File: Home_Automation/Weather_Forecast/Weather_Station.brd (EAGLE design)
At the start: 30 x 20 mm, 14 parts, among them U1 SHT4X, U2 DPS310

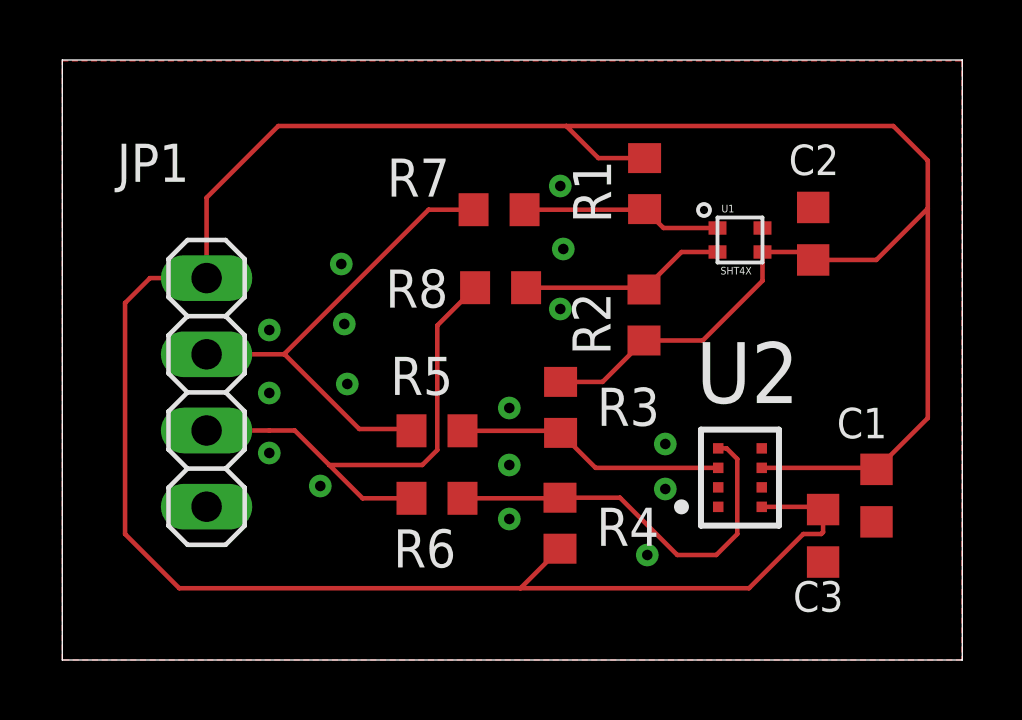
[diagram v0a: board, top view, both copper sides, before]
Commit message: New version: Re-design for better working and added a LED for indicating power
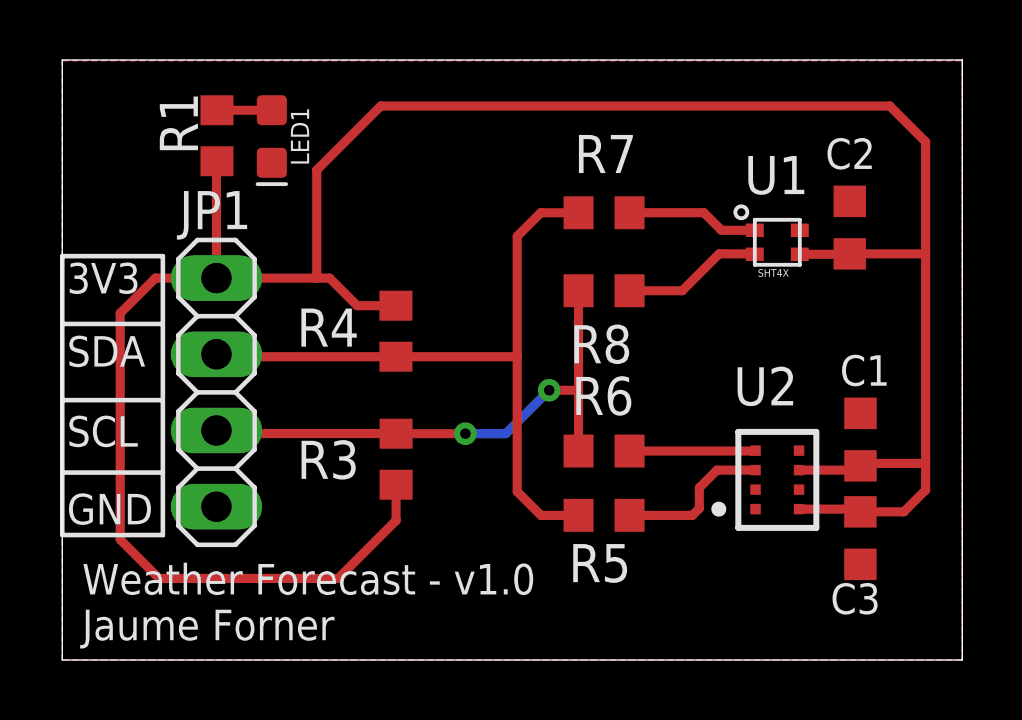
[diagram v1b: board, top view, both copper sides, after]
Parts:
- removed R2: 10k, rcl:R0603
- added LED1: (no value), SparkFun-LED:LED-0603
- R1: value 10k -> 330
- moved R1 14.3 mm to (5.16, 17.5)
- moved R4 8.42 mm to (11.1, 11.0), turned to 90 degrees
- moved R5 6.24 mm to (18.1, 4.82)
- moved R6 5.79 mm to (18.1, 6.96)
- moved R3 5.75 mm to (11.1, 6.69), turned to 270 degrees
- moved R7 3.50 mm to (18.1, 14.9)
- moved R8 3.45 mm to (18.1, 12.3)
- moved C1 1.94 mm to (26.6, 7.35), turned to 90 degrees
- moved C3 1.25 mm to (26.6, 4.06)
- moved U1 1.25 mm to (23.8, 13.9)
- moved U2 1.25 mm to (23.8, 6.00)
- moved C2 1.24 mm to (26.2, 14.4)
- moved JP1 0.33 mm to (5.14, 8.92)
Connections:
- new net N$15: LED1.A, R1.2
- net 3V3: now also R1.1; no longer R1.2, R2.2
- net GND: now also LED1.C
- net N$1: no longer R4.1
- net N$2: no longer R3.1
- net N$3: no longer R1.1
- net N$4: no longer R2.1
- net SCL: now also R3.1
- net SDA: now also R4.1
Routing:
- net 3V3: track 101.8 -> 83.2 mm
- net N$1: track 13.5 -> 4.21 mm
- net SDA: track 16.2 -> 23.3 mm
- net N$2: track 9.04 -> 5.23 mm
- net N$3: track 6.70 -> 4.42 mm
- net N$4: track 6.92 -> 4.69 mm
- net N$15: track 0.00 -> 1.83 mm
- net SCL: track 17.5 -> 18.3 mm, vias 0 -> 2
- added copper zone on layer 16, net GND
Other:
- board text added: "3V3"
- board text added: "GND"
- board text added: "SCL"
- board text added: "SDA"
- board text added: "Weather Forecast - v1.0 Jaume Forner"
